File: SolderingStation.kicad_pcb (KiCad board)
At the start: 2 copper layers, 50 x 50 mm, 51 parts, among them J1 POWER, J2 SW, J3 I2C, J4 IRON, J5 ENCODER, Q1 BC817, Q2 Q_NMOS_GDSD, SW1 SW_SPST, U1 AP1117-33, U2 TLC272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

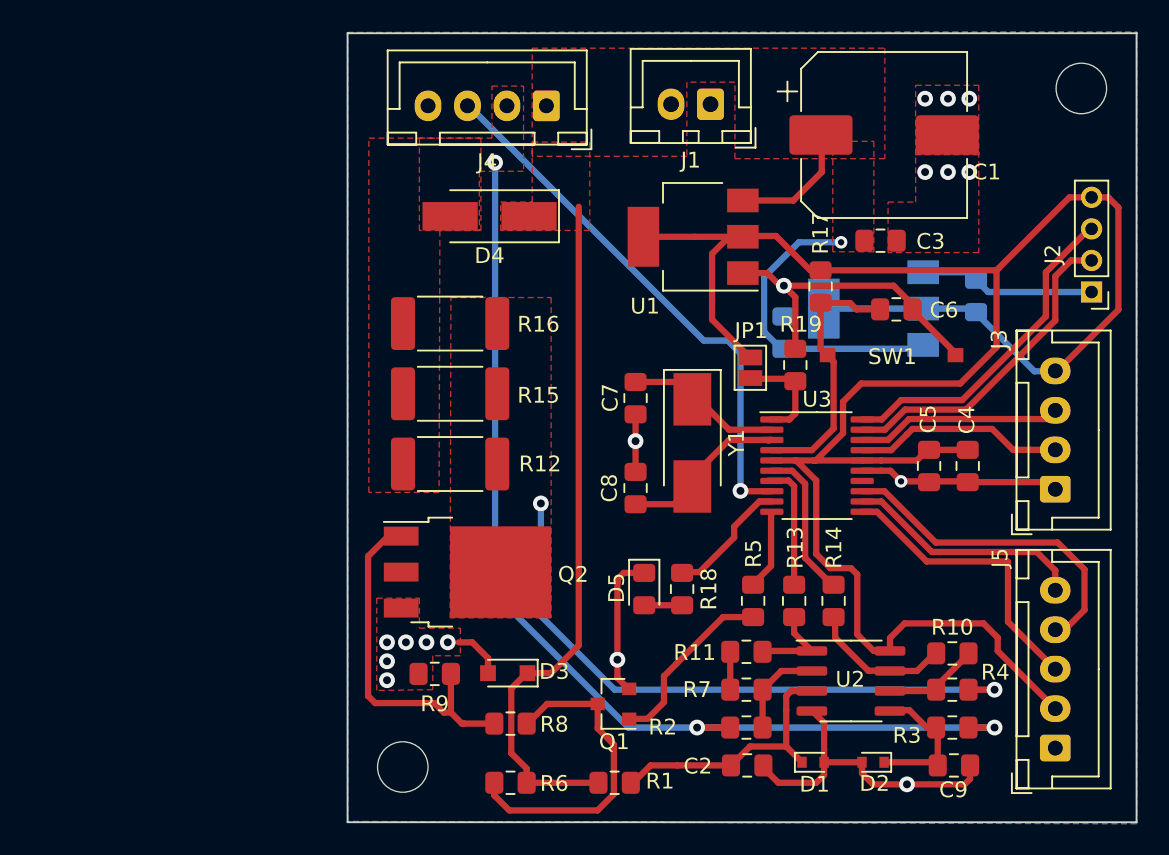
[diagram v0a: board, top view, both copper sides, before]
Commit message: A mad change has commited
N Channel mosfet was creating such agony that no one should ever be exposed to. Switch to P channel mos and changed the overall  shape to more like a rectangle.
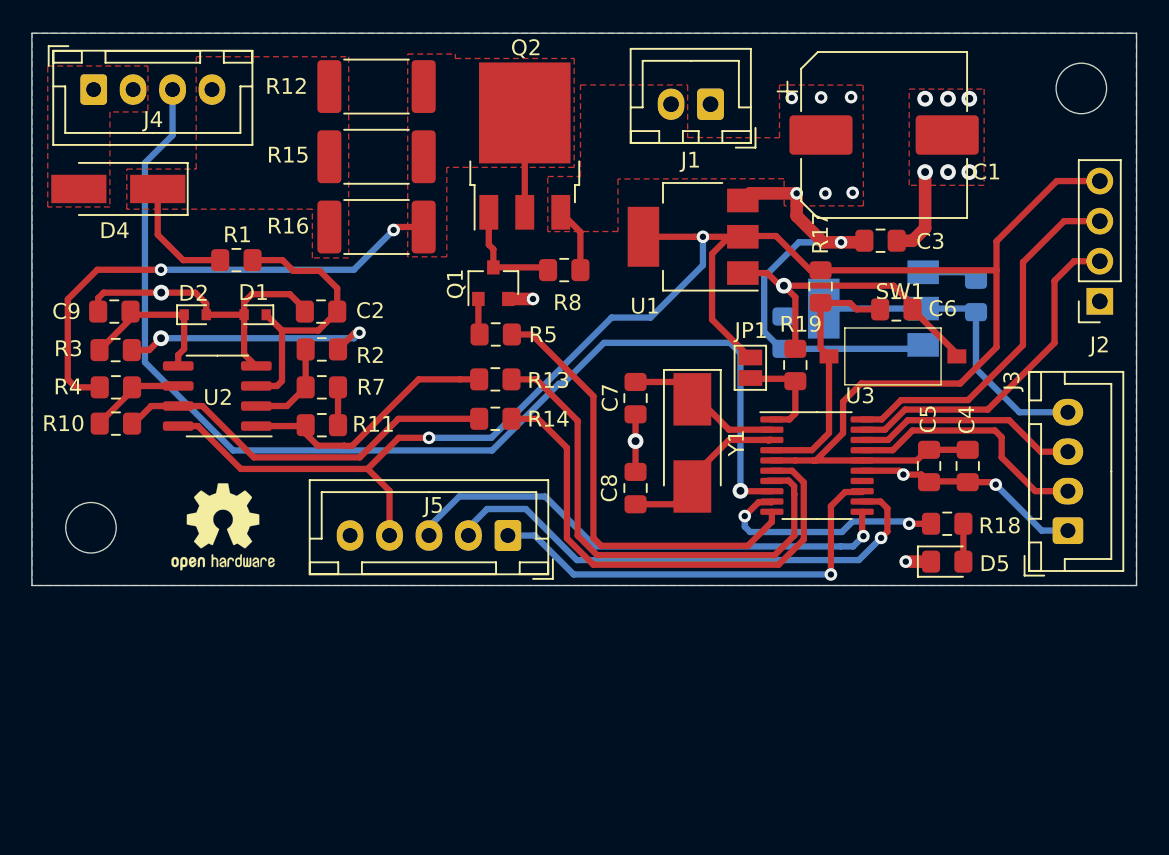
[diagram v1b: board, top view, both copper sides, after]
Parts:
- removed D3: 10V, Diode_SMD:D_SOD-323_HandSoldering
- removed R6: 10K, Resistor_SMD:R_0805_2012Metric_Pad1.15x1.40mm_HandSolder
- removed R9: 470K, Resistor_SMD:R_0805_2012Metric_Pad1.15x1.40mm_HandSolder
- added REF**: OSHW-Logo2_7.3x6mm_SilkScreen, Symbol:OSHW-Logo2_7.3x6mm_SilkScreen, F.Cu at (37.4, 81.0)
- C10, C2, C3, C5, C9: value C -> 100nF
- C11, C4: value C -> 10uF
- C6: value C -> 100nf
- C7, C8: value C -> 27pF
- J2: footprint Connector_PinHeader_2.00mm:PinHeader_1x04_P2.00mm_Vertical -> Connector_PinSocket_2.54mm:PinSocket_1x04_P2.54mm_Vertical
- Q2: value Q_NMOS_GDSD -> Q_PMOS_GDS; footprint Package_TO_SOT_SMD:TO-252-3_TabPin4 -> Package_TO_SOT_SMD:TO-252-3_TabPin2
- R8: value 10R -> 10K
- SW1: footprint sw_tact:L-KLS7-TS3611-2.5-180-T -> SW_TACT:L-KLS7-TS3611-2.5-180-T
- moved C9 60.5 mm to (30.5, 67.3), turned to 180 degrees
- moved R3 58.2 mm to (30.6, 69.8)
- moved R4 56.4 mm to (30.6, 72.1), turned to 180 degrees
- moved R10 55.0 mm to (30.6, 74.4), turned to 180 degrees
- moved D2 51.5 mm to (35.6, 67.5), turned to 0 degrees
- moved D1 45.3 mm to (39.4, 67.5), turned to 180 degrees
- moved U2 44.0 mm to (37.0, 72.7), turned to 180 degrees
- moved R1 40.9 mm to (38.3, 64.1)
- moved C2 39.5 mm to (43.6, 67.3), turned to 180 degrees
- moved J5 37.2 mm to (55.5, 81.5), turned to 180 degrees
- moved R2 36.0 mm to (43.7, 69.7), turned to 0 degrees
- moved R7 33.0 mm to (43.7, 72.1), turned to 180 degrees
- moved R11 30.5 mm to (43.7, 74.5), turned to 0 degrees
- moved R8 28.9 mm to (59.0, 64.7)
- moved J4 28.7 mm to (29.2, 53.3), turned to 0 degrees
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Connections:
- C1 pad 1: IRON_P -> +24V
- C10 pad 1: IRON_P -> +24V
- C3 pad 1: IRON_P -> +24V
- D4 pad 2: IRON_N -> GND
- J1 pad 2: IRON_P -> +24V
- J4 pad 1: IRON_P -> GND
- J4 pad 2: IRON_N -> GND
- J4 pad 4: GND -> IRON_P
- J5 pad 1: GND -> ENC_BTN
- J5 pad 2: +3V3 -> ENC_B
- J5 pad 3: ENC_BTN -> ENC_A
- J5 pad 4: ENC_B -> +3V3
- J5 pad 5: ENC_A -> GND
- Q2 pad 1: Net-(Q2-Pad1) -> Net-(Q1-Pad3)
- Q2 pad 2: (no net) -> SHUNT_P
- Q2 pad 3: GND -> +24V
- R12 pad 1: IRON_N -> SHUNT_P
- R12 pad 2: SHUNT_N -> IRON_P
- R15 pad 1: IRON_N -> SHUNT_P
- R15 pad 2: SHUNT_N -> IRON_P
- R16 pad 1: IRON_N -> SHUNT_P
- R16 pad 2: SHUNT_N -> IRON_P
- R2 pad 2: IRON_N -> GND
- R3 pad 2: IRON_N -> GND
- R4 pad 2: SHUNT_N -> SHUNT_P
- R8 pad 1: Net-(Q2-Pad1) -> Net-(Q1-Pad3)
- R8 pad 2: Net-(Q1-Pad3) -> +24V
- U1 pad 3: IRON_P -> +24V
- U3 pad 11: ENC_BTN -> ENC_A
- U3 pad 12: ENC_A -> ENC_B
- U3 pad 13: ENC_B -> ENC_BTN
- U3 pad 14: (no net) -> Net-(U3-Pad14)
- U4 pad 3: IRON_P -> +24V
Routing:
- net IRON_N: track 66.3 -> 0.00 mm, vias 3 -> 0
- net IRON_P: track 71.5 -> 7.53 mm, vias 1 -> 0
- net SHUNT_N: track 39.5 -> 0.00 mm, vias 2 -> 0
- net SHUNT_P: track 0.00 -> 38.1 mm, vias 0 -> 2
- net TILT: track 34.6 -> 71.9 mm
- net +24V: track 0.00 -> 33.7 mm, vias 0 -> 7
- net TEMP: track 8.04 -> 32.3 mm
- net PWM: track 5.03 -> 28.6 mm
- net CURR: track 9.68 -> 32.4 mm
- net Net-(Q2-Pad1): track 22.7 -> 0.00 mm
- net ENC_A: track 15.3 -> 32.0 mm, vias 0 -> 1
- net Net-(R10-Pad1): track 8.86 -> 24.7 mm
- net Net-(Q1-Pad3): track 20.3 -> 7.15 mm
- net ENC_B: track 21.1 -> 32.9 mm, vias 0 -> 1
- net Net-(R11-Pad1): track 5.70 -> 16.7 mm
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- added copper zone on F.Cu, net +24V
- added copper zone on F.Cu, net SHUNT_P
- removed copper zone on F.Cu, net IRON_N
- removed copper zone on F.Cu, net SHUNT_N
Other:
- board size 50 x 50 mm -> 70 x 35 mm
